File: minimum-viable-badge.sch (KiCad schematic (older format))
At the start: 43 parts, among them P1 BATTERY, P11 MECH, P12 MECH, P13 MECH, P2 USB, P3 CONN_01X14, P4 eInk, P5 CONN_01X10, P6 POT_LONG, P8 CONN_01X14, P9 POT_SHORT, Q1 S8050, Q2 S8050, SW1 PRGM, SW2 RESET, U1 CP2102, U2 ESP32-WROOM

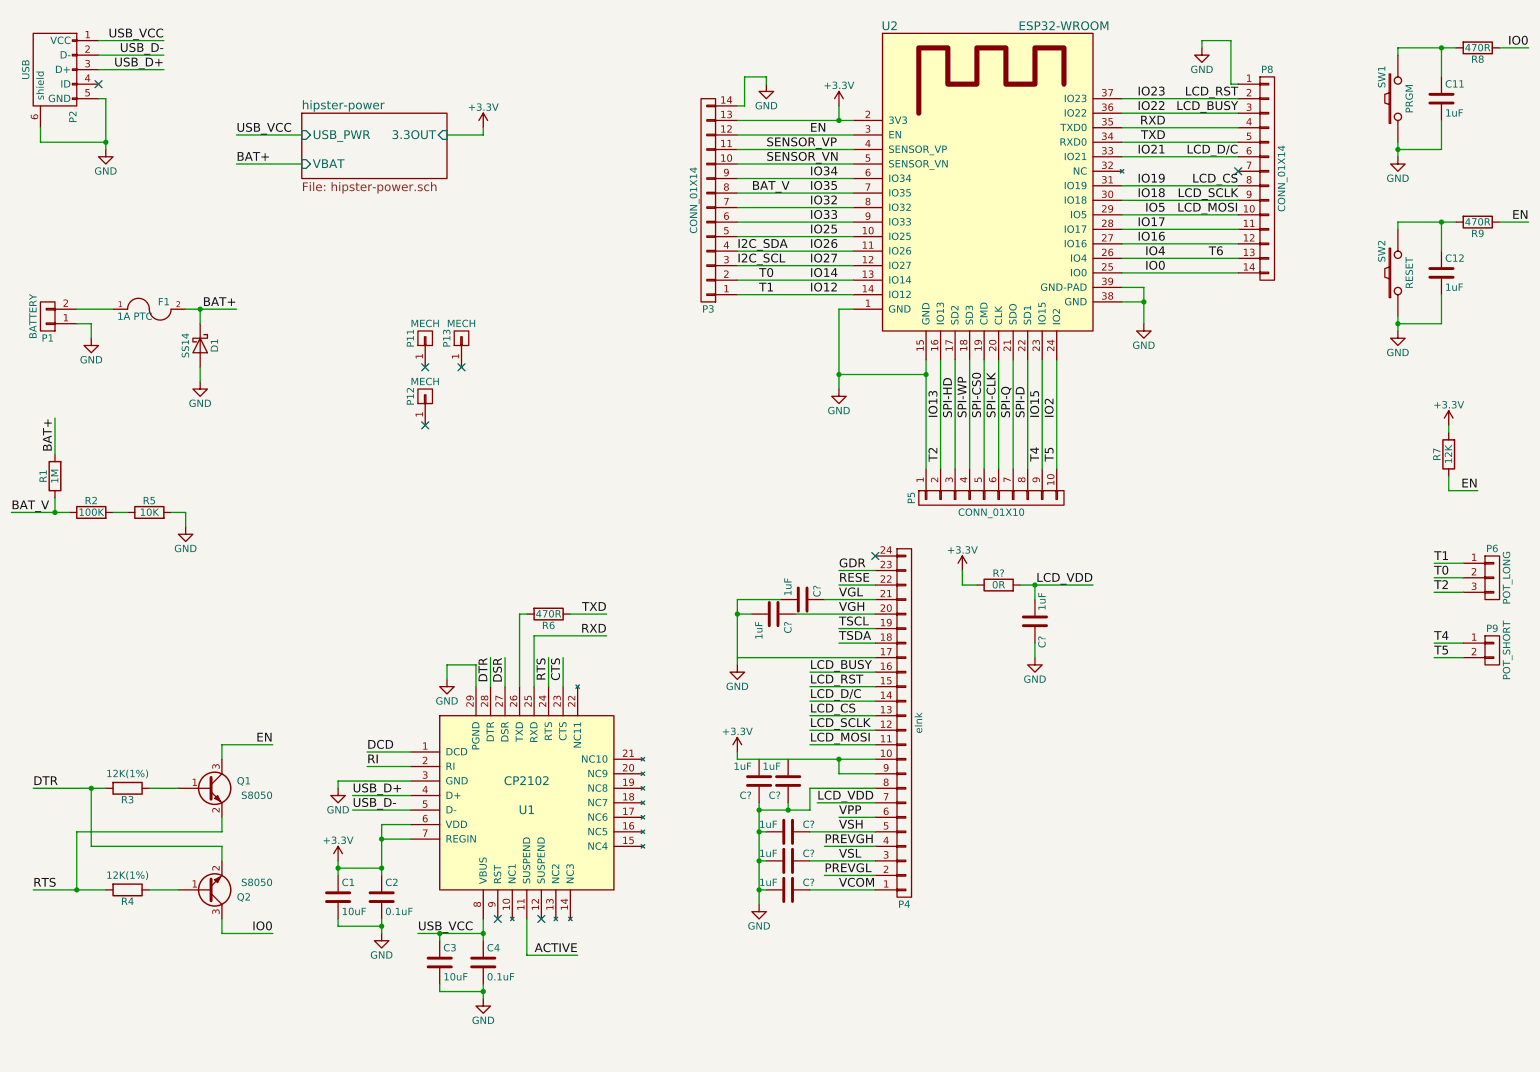
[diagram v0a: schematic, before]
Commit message: Extra touch buttons
and edge connector!
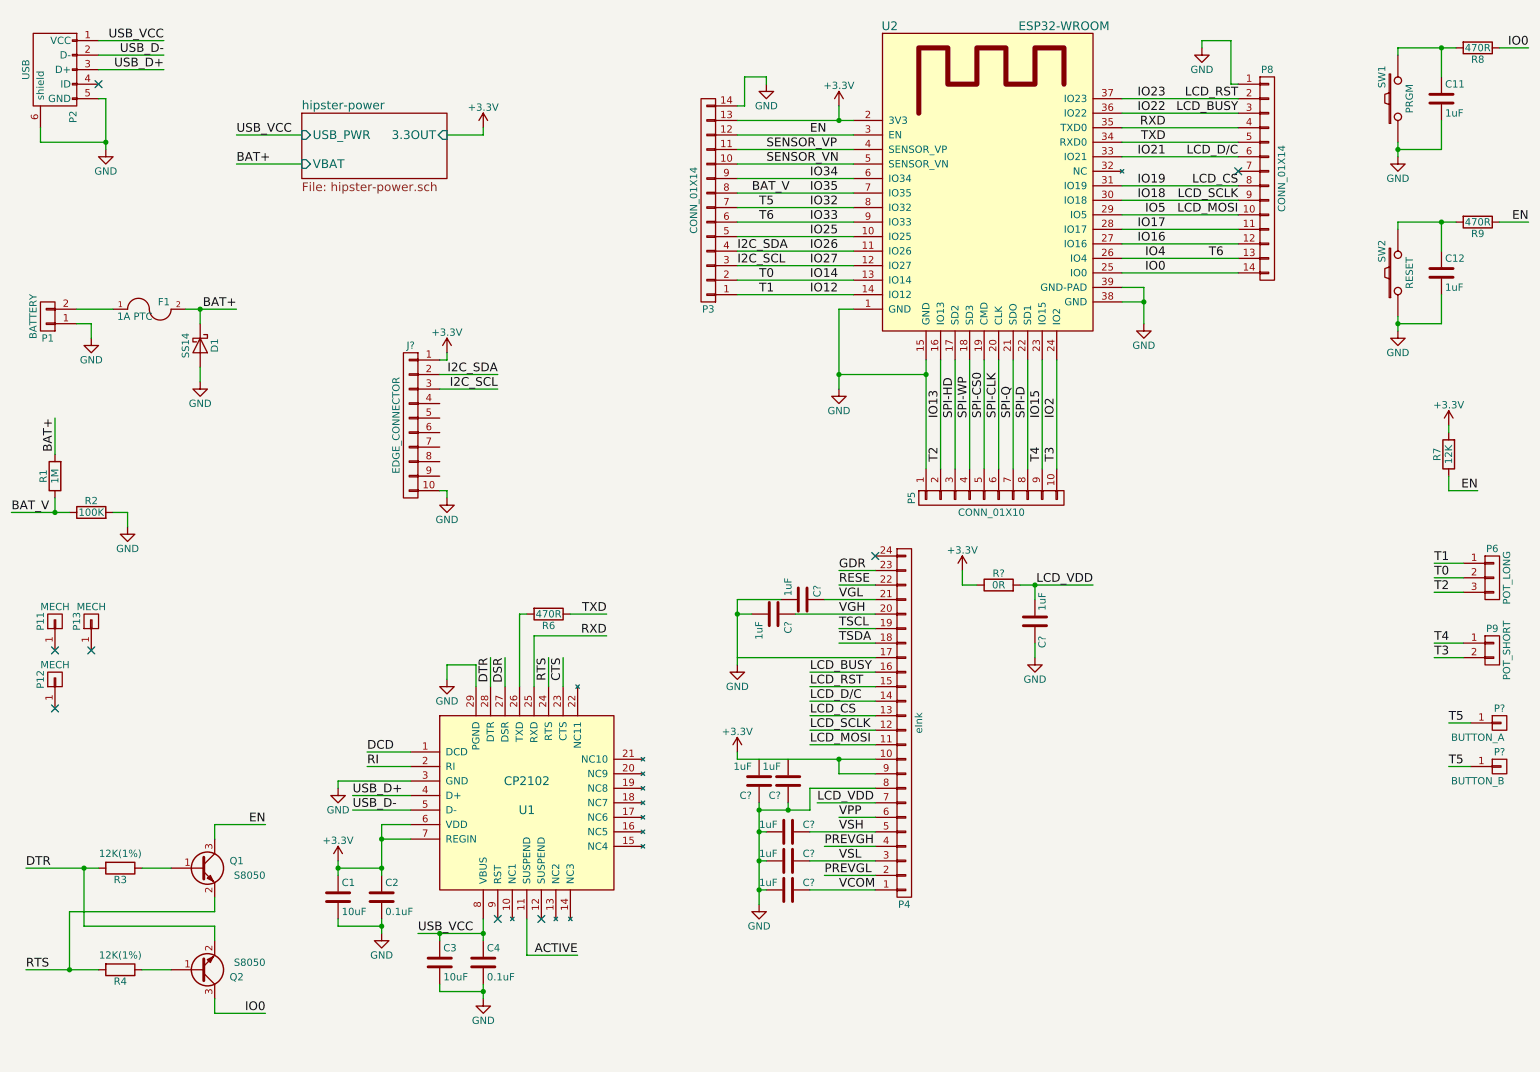
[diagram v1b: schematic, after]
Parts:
- removed R5: 10K, Resistors_SMD:R_0603_HandSoldering, symbol R
- added J?: EDGE_CONNECTOR, symbol CONN_01X10
- added P?: BUTTON_A, Mounting_Holes:MountingHole_3.2mm_M3_Pad, symbol CONN_01X01
- added P?: BUTTON_B, Mounting_Holes:MountingHole_3.2mm_M3_Pad, symbol CONN_01X01
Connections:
- net IO4 is gone; now on net IO33: P8.13 (P13), U2.26 (IO4)
- net +3V3: now also J?.1 (P1)
- net GND: now also R2.2, J?.10 (P10)
- net I2C_SCL: now also J?.3 (P3)
- net I2C_SDA: now also J?.2 (P2)
- net IO32: now also P?.1 (P1), P?.1 (P1)
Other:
- moved on the sheet: P11, P12, P13, Q1, Q2, R3, R4

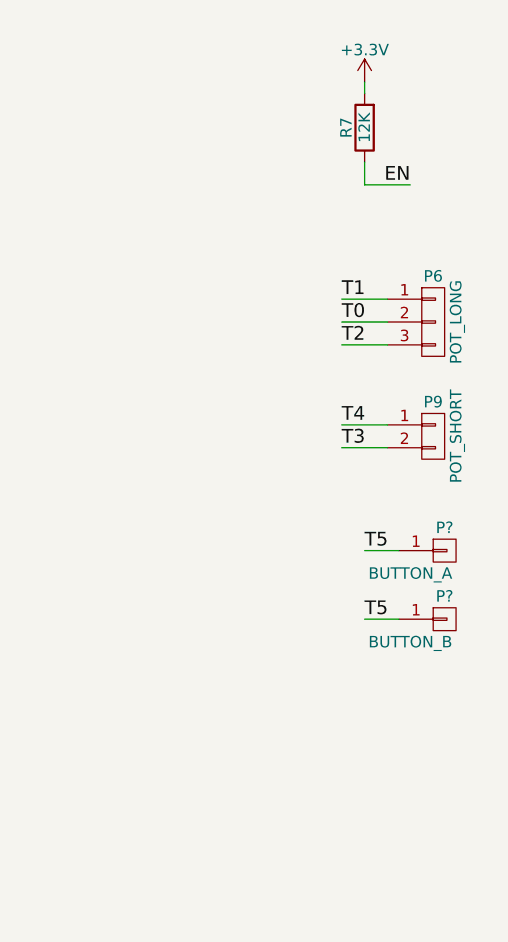
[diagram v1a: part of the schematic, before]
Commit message: Add capacitor to EN pin
Prevents problems with auto-reset
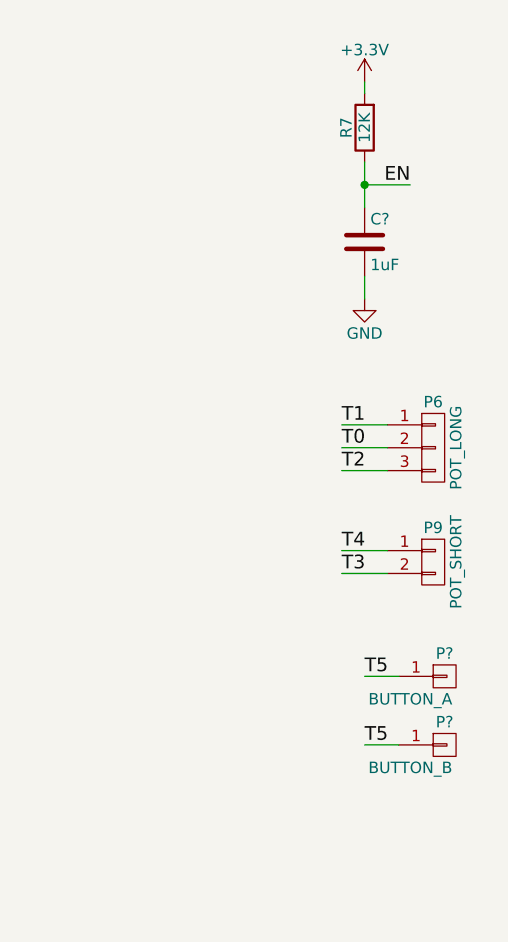
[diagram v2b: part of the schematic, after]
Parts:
- added C?: 1uF, Capacitors_SMD:C_0603_HandSoldering, symbol C
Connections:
- net EN: now also C?.1
- net GND: now also C?.2
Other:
- moved on the sheet: P6, P9, P?
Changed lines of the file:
@@
 	1    0    0    1
 $EndComp
-Text Label 10400 4550 0    60   ~ 0
+Text Label 10400 5100 0    60   ~ 0
 T2
-Text Label 10400 4900 0    60   ~ 0
+Text Label 10400 5450 0    60   ~ 0
 T4
-Text Label 10400 5000 0    60   ~ 0
+Text Label 10400 5550 0    60   ~ 0
 T3
 Text Label 600  4000 0    60   ~ 0
@@
 Text Label 5750 2500 0    60   ~ 0
 T1
-Text Label 10400 4450 0    60   ~ 0
+Text Label 10400 5000 0    60   ~ 0
 T0
-Text Label 10400 4350 0    60   ~ 0
+Text Label 10400 4900 0    60   ~ 0
 T1
 $Comp
 L CONN_01X02 P9
 U 1 1 5937169B
-P 10800 4950
-F 0 "P9" H 10800 5100 50  0000 C CNN
-F 1 "POT_SHORT" V 10900 4950 50  0000 C CNN
-F 2 "libs:sense_short" H 10800 4950 50  0001 C CNN
-F 3 "" H 10800 4950 50  0000 C CNN
-	1    10800 4950
+P 10800 5500
+F 0 "P9" H 10800 5650 50  0000 C CNN
+F 1 "POT_SHORT" V 10900 5500 50  0000 C CNN
+F 2 "libs:sense_short" H 10800 5500 50  0001 C CNN
+F 3 "" H 10800 5500 50  0000 C CNN
+	1    10800 5500
 	1    0    0    -1
 $EndComp
@@
 L CONN_01X03 P6
 U 1 1 59A0383A
-P 10800 4450
-F 0 "P6" H 10800 4650 50  0000 C CNN
-F 1 "POT_LONG" V 10900 4450 50  0000 C CNN
-F 2 "libs:sense_long" H 10800 4450 50  0001 C CNN
-F 3 "" H 10800 4450 50  0000 C CNN
-	1    10800 4450
+P 10800 5000
+F 0 "P6" H 10800 5200 50  0000 C CNN
+F 1 "POT_LONG" V 10900 5000 50  0000 C CNN
+F 2 "libs:sense_long" H 10800 5000 50  0001 C CNN
+F 3 "" H 10800 5000 50  0000 C CNN
+	1    10800 5000
 	1    0    0    -1
 $EndComp
@@
 	10500 3450 10500 3400
 Wire Wire Line
-	10500 3750 10500 3850
+	10500 3750 10500 3950
 Wire Wire Line
 	10500 3850 10700 3850
@@
 	6550 5600 6100 5600
 Wire Wire Line
-	10400 4550 10600 4550
-Wire Wire Line
-	10400 4350 10600 4350
-Wire Wire Line
-	10400 4450 10600 4450
+	10400 5100 10600 5100
 Wire Wire Line
 	10400 4900 10600 4900
 Wire Wire Line
 	10400 5000 10600 5000
+Wire Wire Line
+	10400 5450 10600 5450
+Wire Wire Line
+	10400 5550 10600 5550
 Wire Wire Line
 	6550 4400 6300 4400
@@
 L CONN_01X01 P?
 U 1 1 59A413E1
-P 10850 5450
-F 0 "P?" H 10850 5550 50  0000 C CNN
-F 1 "BUTTON_A" H 10700 5350 50  0000 C CNN
-F 2 "Mounting_Holes:MountingHole_3.2mm_M3_Pad" H 10850 5450 50  0001 C CNN
-F 3 "" H 10850 5450 50  0000 C CNN
-	1    10850 5450
+P 10850 6000
+F 0 "P?" H 10850 6100 50  0000 C CNN
+F 1 "BUTTON_A" H 10700 5900 50  0000 C CNN
+F 2 "Mounting_Holes:MountingHole_3.2mm_M3_Pad" H 10850 6000 50  0001 C CNN
+F 3 "" H 10850 6000 50  0000 C CNN
+	1    10850 6000
 	1    0    0    -1
 $EndComp
@@
 L CONN_01X01 P?
 U 1 1 59A41FB4
-P 10850 5750
-F 0 "P?" H 10850 5850 50  0000 C CNN
-F 1 "BUTTON_B" H 10700 5650 50  0000 C CNN
-F 2 "Mounting_Holes:MountingHole_3.2mm_M3_Pad" H 10850 5750 50  0001 C CNN
-F 3 "" H 10850 5750 50  0000 C CNN
-	1    10850 5750
-	1    0    0    -1
-$EndComp
-Text Label 10500 5450 0    60   ~ 0
+P 10850 6300
+F 0 "P?" H 10850 6400 50  0000 C CNN
+F 1 "BUTTON_B" H 10700 6200 50  0000 C CNN
+F 2 "Mounting_Holes:MountingHole_3.2mm_M3_Pad" H 10850 6300 50  0001 C CNN
+F 3 "" H 10850 6300 50  0000 C CNN
+	1    10850 6300
+	1    0    0    -1
+$EndComp
+Text Label 10500 6000 0    60   ~ 0
 T5
-Text Label 10500 5750 0    60   ~ 0
+Text Label 10500 6300 0    60   ~ 0
 T5
 Text Label 5750 1900 0    60   ~ 0
@@
 T6
 Wire Wire Line
-	10650 5450 10500 5450
-Wire Wire Line
-	10650 5750 10500 5750
+	10650 6000 10500 6000
+Wire Wire Line
+	10650 6300 10500 6300
 $Comp
 L CONN_01X10 J?
@@
 Wire Wire Line
 	3550 3150 3950 3150
+Connection ~ 10500 3850
+Wire Wire Line
+	10500 4250 10500 4350
+$Comp
+L GND #PWR?
+U 1 1 59A4F54D
+P 10500 4350
+F 0 "#PWR?" H 10500 4100 50  0001 C CNN
+F 1 "GND" H 10500 4200 50  0000 C CNN
+F 2 "" H 10500 4350 50  0001 C CNN
+F 3 "" H 10500 4350 50  0001 C CNN
+	1    10500 4350
+	1    0    0    -1
+$EndComp
+$Comp
+L C C?
+U 1 1 59A4FE66
+P 10500 4100
+F 0 "C?" H 10525 4200 50  0000 L CNN
+F 1 "1uF" H 10525 4000 50  0000 L CNN
+F 2 "Capacitors_SMD:C_0603_HandSoldering" H 10538 3950 50  0001 C CNN
+F 3 "" H 10500 4100 50  0000 C CNN
+	1    10500 4100
+	1    0    0    -1
+$EndComp
 $EndSCHEMATC

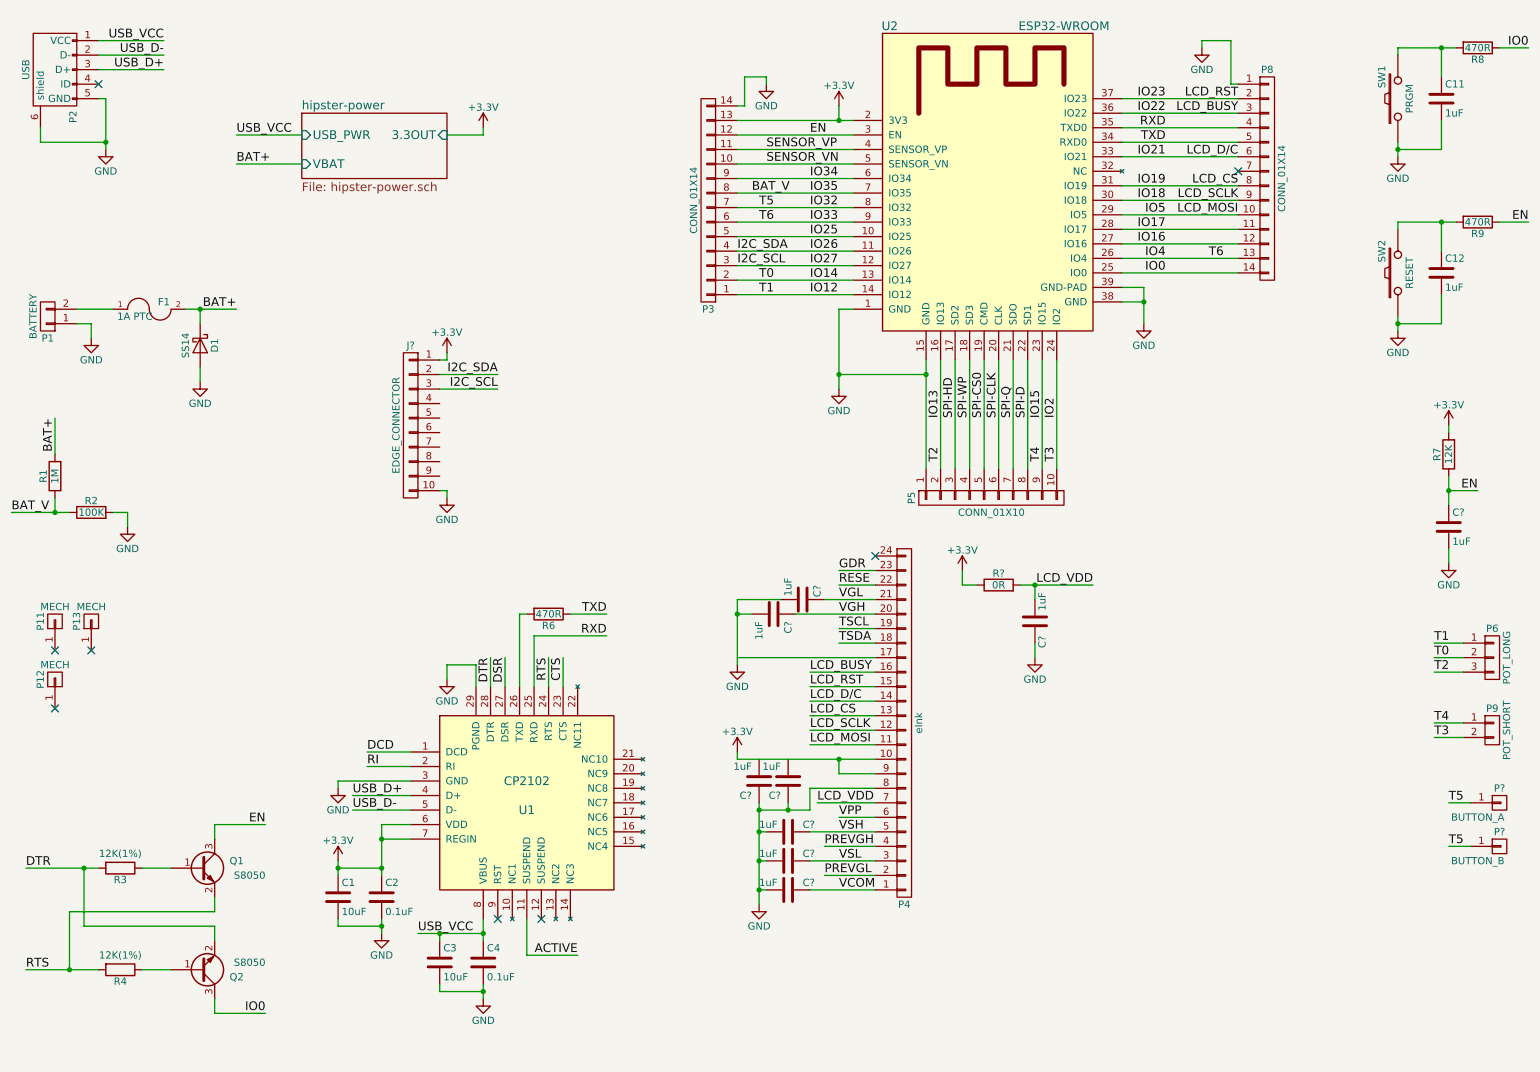
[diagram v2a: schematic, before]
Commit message: Arrange & label schematic, pass ERC
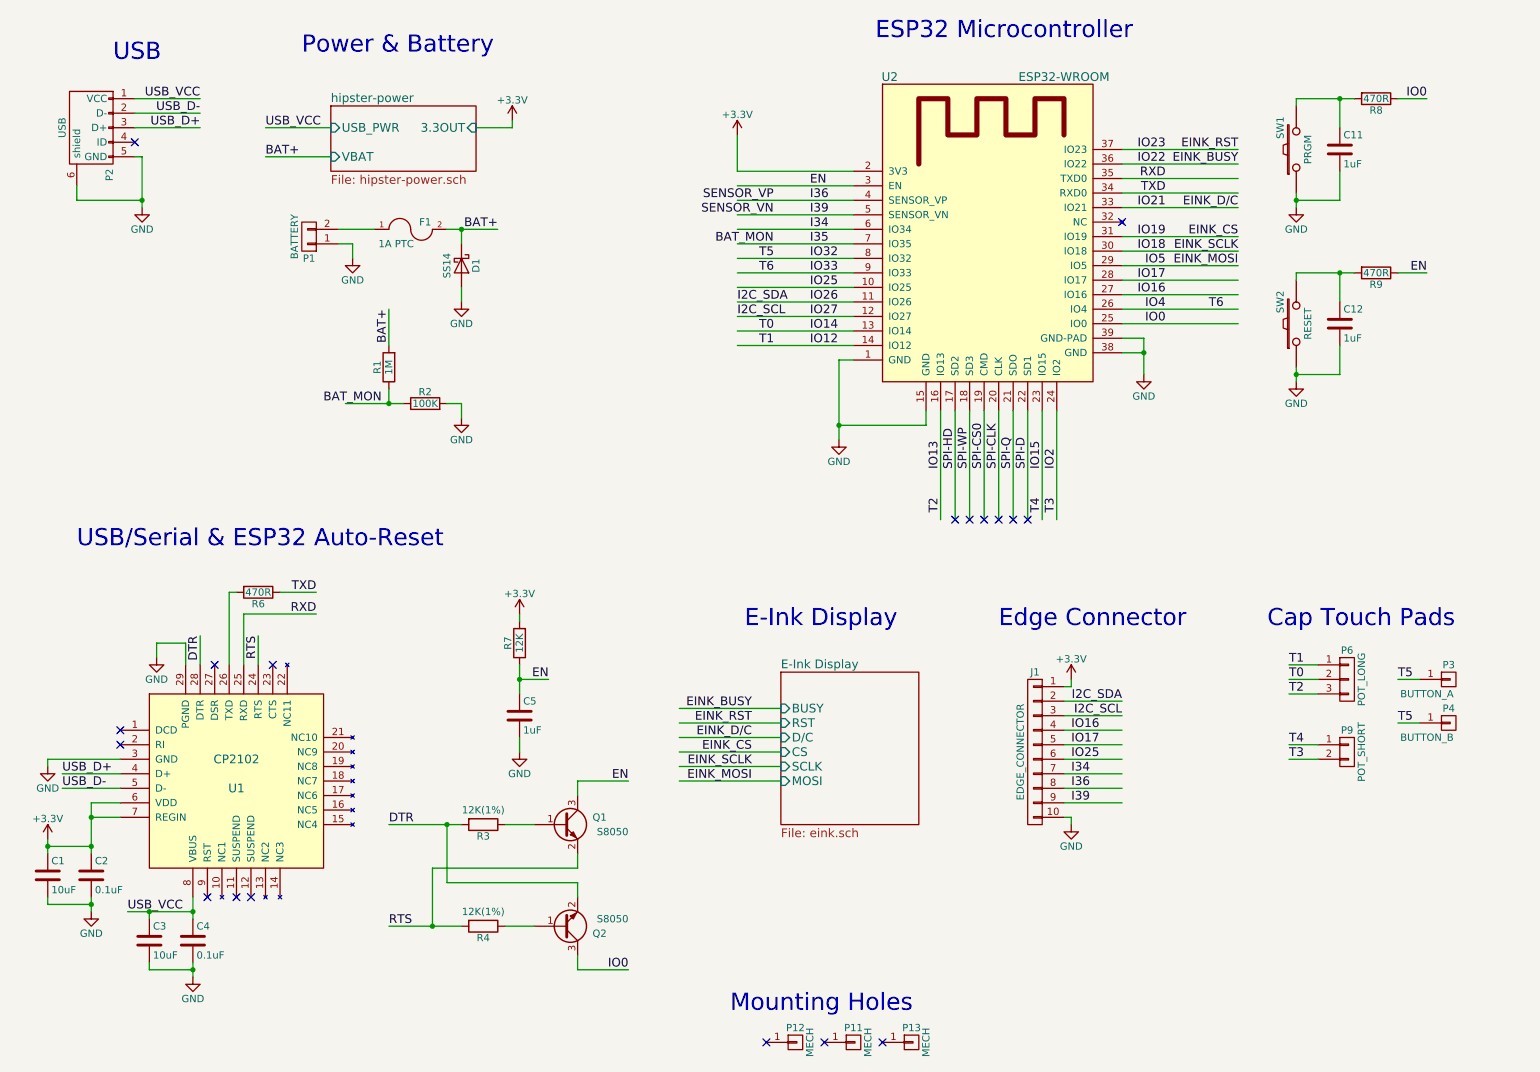
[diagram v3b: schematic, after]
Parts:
- removed C? (x8): 1uF, Capacitors_SMD:C_0603_HandSoldering, symbol C
- removed P3, P8: CONN_01X14, symbol CONN_01X14
- removed P4: eInk, libs:FPC_0.5mm_Pitch_24_Pin, symbol CONN_01X24
- removed P5: CONN_01X10, symbol CONN_01X10
- removed R?: 0R, Resistors_SMD:R_0603_HandSoldering, symbol R
- gave numbers to parts that had none: 4
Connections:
- net labels added: BAT_MON, EINK_BUSY, EINK_CS, EINK_D/C, EINK_MOSI, EINK_RST, EINK_SCLK, I34, I35, I36, I39
- net labels removed: ACTIVE, BAT_V, CTS, DCD, DSR, GDR, IO34, IO35, LCD_BUSY, LCD_CS, LCD_D/C, LCD_MOSI, LCD_RST, LCD_SCLK, LCD_VDD, PREVGH, PREVGL, RESE, RI, TSCL, TSDA, VCOM, VGH, VGL, VPP, VSH, VSL
- wire segments 191 -> 149
- no-connect marks 8 -> 18
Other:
- note added: "Cap Touch Pads"
- note added: "E-Ink Display"
- note added: "ESP32 Microcontroller"
- note added: "Edge Connector"
- note added: "Mounting Holes"
- note added: "Power & Battery"
- note added: "USB"
- note added: "USB/Serial & ESP32 Auto-Reset"
- moved on the sheet: C1, C11, C12, C2, C3, C4, C5, D1, F1, J1, P1, P11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
